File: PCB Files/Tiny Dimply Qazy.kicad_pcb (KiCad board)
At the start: 2 copper layers, 200 x 76.2 mm, 93 parts, among them J1 Conn_01x04_Male, J2 USB_C_Receptacle_USB2.0, Q1 2N7002, SW1 B/R, U1 STM32F072CBTx, U2 XC6206PxxxMR-Regulator_Linear, U3 USBLC6-2SC6

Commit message: Add prototype production changes
* R4, R5 to 0603 (as requested during prototype PCBA)
* Replace C_VDD2 with C_VDD3
* Add missing ground connections for R1, R2
* Move silk texts to the back
* Centered big silk text
* Add Molex EZMate Pico 4-pin header close to the JST SH header
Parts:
- removed the C_VDD2 at (44.1, 97.3)
- added J3: Conn_01x04_Male, Connector_Molex:Molex_Pico-EZmate_78171-0004_1x04-1MP_P1.20mm_Vertical, B.Cu at (207.9, 70.7)
- G***, Geon: moved to B.Cu
- MX32: footprint MX_Only:MXOnly-1.25U-NoLED -> MX_Only:MXOnly-1U-NoLED
- R4, R5: footprint Resistor_SMD:R_0402_1005Metric -> Resistor_SMD:R_0603_1608Metric
- moved G*** 9.52 mm to (139.7, 108.7), turned to 180 degrees
- turned Geon to 180 degrees
- renumbered C_VDD3 to C_VDD2
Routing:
- net GND: track 211.3 -> 220.7 mm, vias 10 -> 12
- net +5V: track 39.1 -> 41.2 mm
- net DBUS+: track 18.9 -> 20.9 mm
- net DBUS-: track 17.6 -> 19.6 mm
- net +3V3: track 255.8 -> 255.0 mm

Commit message: Change MX32 to 1.25U in the schematic
No real changes to production files
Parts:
- MX32: footprint MX_Only:MXOnly-1U-NoLED -> MX_Only:MXOnly-1.25U-NoLED
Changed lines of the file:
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@@
       (net 71 "B12") (pinfunction "ROW") (pintype "passive"))
   )
-  (footprint "MX_Only:MXOnly-1U-NoLED" (layer "F.Cu")
+  (footprint "MX_Only:MXOnly-1.25U-NoLED" (layer "F.Cu")
     (at 184.94375 122.2375)
     (property "Field4" "Meta")
@@
       (effects (font (size 1 1) (thickness 0.15)))
     )
+    (fp_line (start 7 -7) (end 7 -5) (layer "Dwgs.User") (width 0.15))
+    (fp_line (start -7 -7) (end -7 -5) (layer "Dwgs.User") (width 0.15))
+    (fp_line (start -11.90625 -9.525) (end 11.90625 -9.525) (layer "Dwgs.User") (width 0.15))
+    (fp_line (start 5 -7) (end 7 -7) (layer "Dwgs.User") (width 0.15))
+    (fp_line (start -7 7) (end -5 7) (layer "Dwgs.User") (width 0.15))
     (fp_line (start -5 -7) (end -7 -7) (layer "Dwgs.User") (width 0.15))
-    (fp_line (start -9.525 -9.525) (end 9.525 -9.525) (layer "Dwgs.User") (width 0.15))
-    (fp_line (start 5 -7) (end 7 -7) (layer "Dwgs.User") (width 0.15))
-    (fp_line (start -9.525 9.525) (end -9.525 -9.525) (layer "Dwgs.User") (width 0.15))
-    (fp_line (start 9.525 -9.525) (end 9.525 9.525) (layer "Dwgs.User") (width 0.15))
+    (fp_line (start -11.90625 9.525) (end 11.90625 9.525) (layer "Dwgs.User") (width 0.15))
+    (fp_line (start 7 7) (end 7 5) (layer "Dwgs.User") (width 0.15))
+    (fp_line (start -11.90625 9.525) (end -11.90625 -9.525) (layer "Dwgs.User") (width 0.15))
     (fp_line (start -7 5) (end -7 7) (layer "Dwgs.User") (width 0.15))
-    (fp_line (start -7 7) (end -5 7) (layer "Dwgs.User") (width 0.15))
     (fp_line (start 5 7) (end 7 7) (layer "Dwgs.User") (width 0.15))
-    (fp_line (start -7 -7) (end -7 -5) (layer "Dwgs.User") (width 0.15))
-    (fp_line (start 9.525 9.525) (end -9.525 9.525) (layer "Dwgs.User") (width 0.15))
-    (fp_line (start 7 -7) (end 7 -5) (layer "Dwgs.User") (width 0.15))
-    (fp_line (start 7 7) (end 7 5) (layer "Dwgs.User") (width 0.15))
+    (fp_line (start 11.90625 -9.525) (end 11.90625 9.525) (layer "Dwgs.User") (width 0.15))
+    (pad "" np_thru_hole circle (at 0 0) (size 3.9878 3.9878) (drill 3.9878) (layers *.Cu *.Mask))
     (pad "" np_thru_hole circle (at -5.08 0 48.0996) (size 1.75 1.75) (drill 1.75) (layers *.Cu *.Mask))
     (pad "" np_thru_hole circle (at 5.08 0 48.0996) (size 1.75 1.75) (drill 1.75) (layers *.Cu *.Mask))
-    (pad "" np_thru_hole circle (at 0 0) (size 3.9878 3.9878) (drill 3.9878) (layers *.Cu *.Mask))
     (pad "1" thru_hole circle (at -3.81 -2.54) (size 2.25 2.25) (drill 1.47) (layers *.Cu *.Mask)
       (net 77 "Net-(D13-Pad2)") (pinfunction "COL") (pintype "passive"))

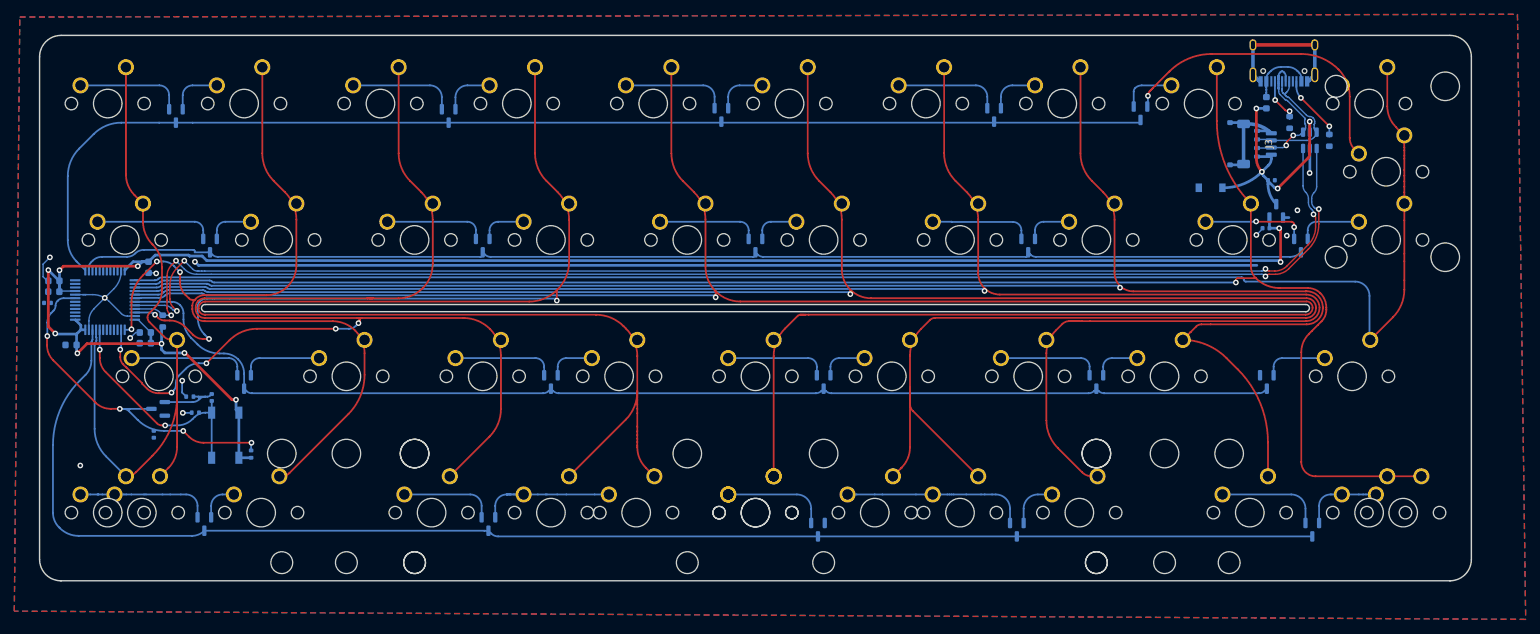
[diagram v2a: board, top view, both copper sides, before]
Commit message: Fix outline and bottom row switch positions c/o @ASH-ART
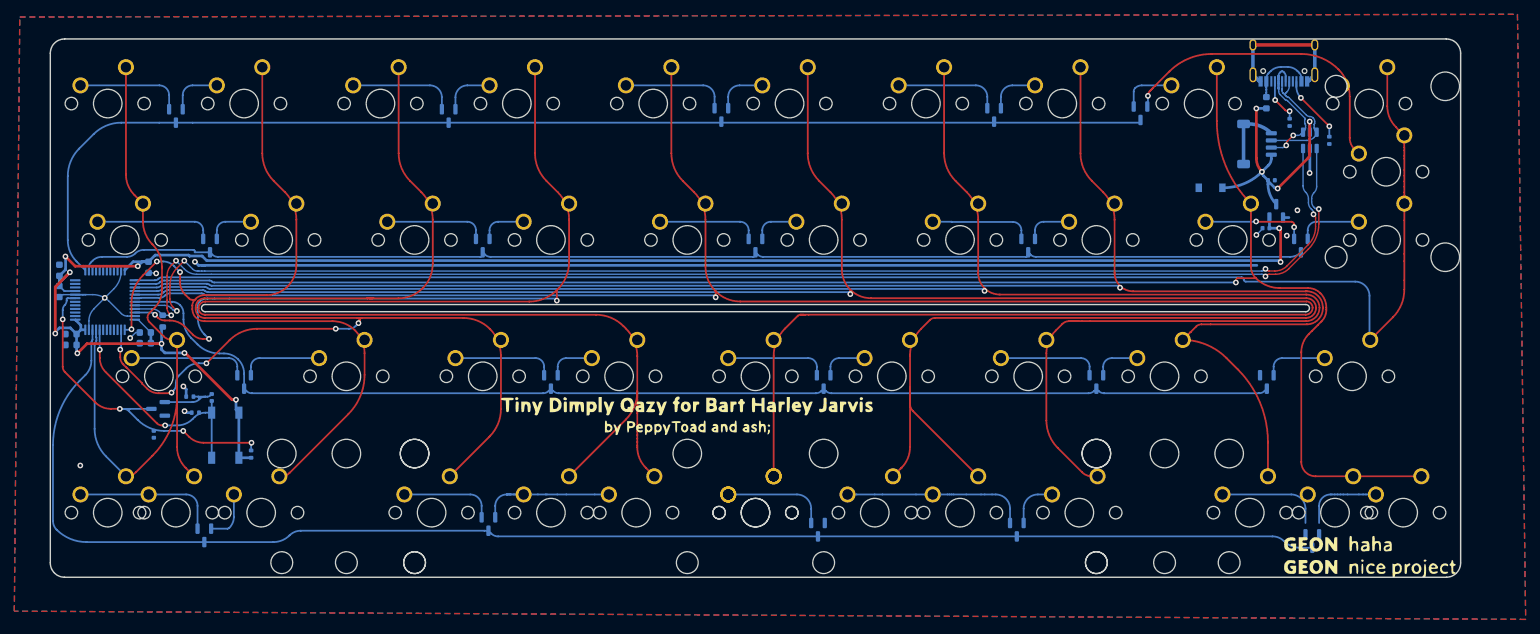
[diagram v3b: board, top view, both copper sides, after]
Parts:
- removed the C2 at (40.8, 92.9)
- removed J3: Conn_01x04_Male, Connector_Molex:Molex_Pico-EZmate_78171-0004_1x04-1MP_P1.20mm_Vertical
- added C_VDD2: 100n, Capacitor_SMD:C_0603_1608Metric, B.Cu at (44.1, 97.3)
- G***, Geon: moved to F.Cu
- R4, R5: footprint Resistor_SMD:R_0603_1608Metric -> Resistor_SMD:R_0402_1005Metric
- moved G*** 9.52 mm to (130.2, 108.7), turned to 0 degrees
- moved MX39 4.76 mm to (220.7, 122.2)
- moved MX1 4.76 mm to (58.7, 122.2)
- moved C_VDDA1 1.67 mm to (42.5, 88.4), turned to 90 degrees
- moved D17 1.59 mm to (217.5, 126.2)
- moved D4 1.59 mm to (62.7, 125.4)
- moved C_VDDA2 0.77 mm to (42.4, 91.3), turned to -90 degrees
- turned Geon to 0 degrees
- renumbered C_VDD2 to C_VDD3
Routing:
- net GND: track 220.7 -> 211.8 mm, vias 12 -> 11
- net +5V: track 41.2 -> 39.1 mm
- net NRST: track 48.8 -> 46.7 mm
- net DBUS+: track 20.9 -> 18.9 mm
- net DBUS-: track 19.6 -> 17.6 mm
- net Net-(D4-Pad2): track 5.67 -> 7.44 mm
- net Net-(D4-Pad1): track 18.8 -> 20.4 mm
- net Net-(D17-Pad2): track 12.6 -> 11.2 mm
- net B9: track 205.1 -> 206.4 mm
- net +3V3: track 255.0 -> 256.0 mm
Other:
- board size 200 x 76.2 mm -> 197 x 75.2 mm
